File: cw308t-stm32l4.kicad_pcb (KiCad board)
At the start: 2 copper layers, 53 x 65 mm, 18 parts, among them J1 CW308T_CONNBOARD, J2 Conn_02x03_Odd_Even, U1 STM32L432KCUx

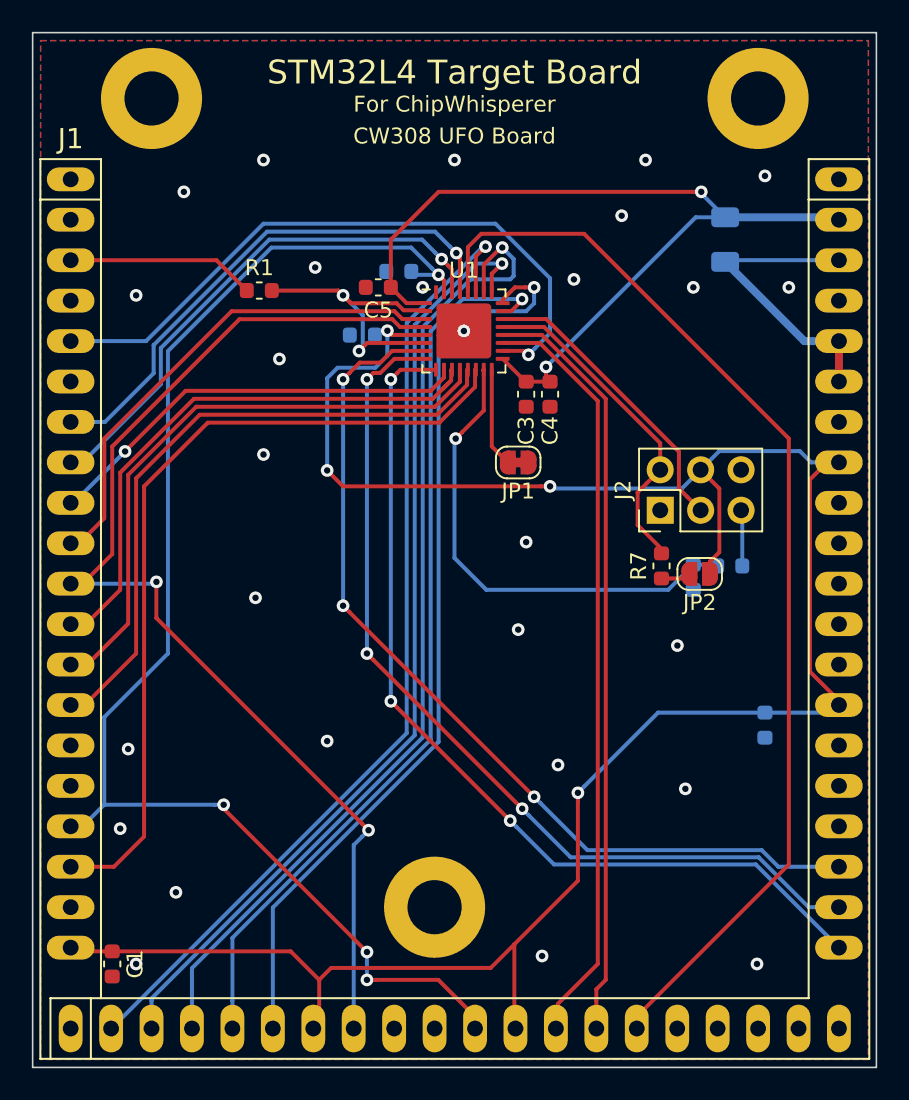
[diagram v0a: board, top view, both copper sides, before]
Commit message: Somewhat better ground
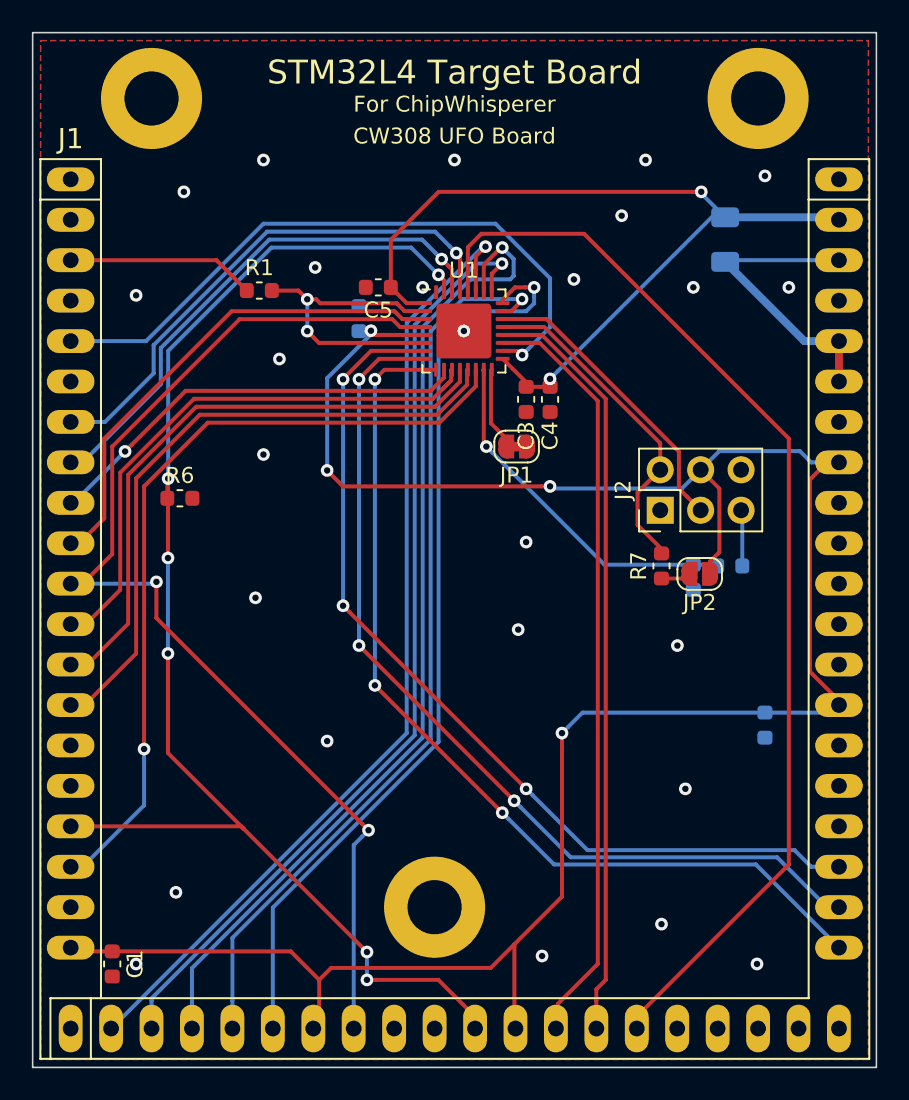
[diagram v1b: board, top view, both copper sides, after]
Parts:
- R6: moved to F.Cu
- moved R6 19.8 mm to (130.8, 89.2), turned to 0 degrees
- moved C6 1.06 mm to (142.0, 78.0), turned to 90 degrees
- moved JP1 1.00 mm to (151.9, 86.0)
- moved C3 0.32 mm to (152.5, 83.0)
- moved C4 0.32 mm to (154.0, 83.0)
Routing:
- net Net-(R3-Pad2): track 30.7 -> 22.6 mm
- net VCC: track 141.5 -> 143.3 mm
- net /BOOT0: track 87.7 -> 89.3 mm, vias 4 -> 6
- net /LED3: track 57.9 -> 59.3 mm
- net /CLKI: track 18.6 -> 19.9 mm
- net /SPI_SS: track 51.9 -> 50.7 mm, vias 0 -> 1
- net Net-(JP1-Pad2): track 6.24 -> 5.24 mm
- net /LED2: track 57.7 -> 58.4 mm
- net GND: vias 28 -> 26
